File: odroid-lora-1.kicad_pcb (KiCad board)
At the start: 2 copper layers, 110 x 110 mm, 14 parts, among them J1 ODROID_2x12_GPIO, J2 RASPPI_2x20_GPIO, J3 M0, J4 M1

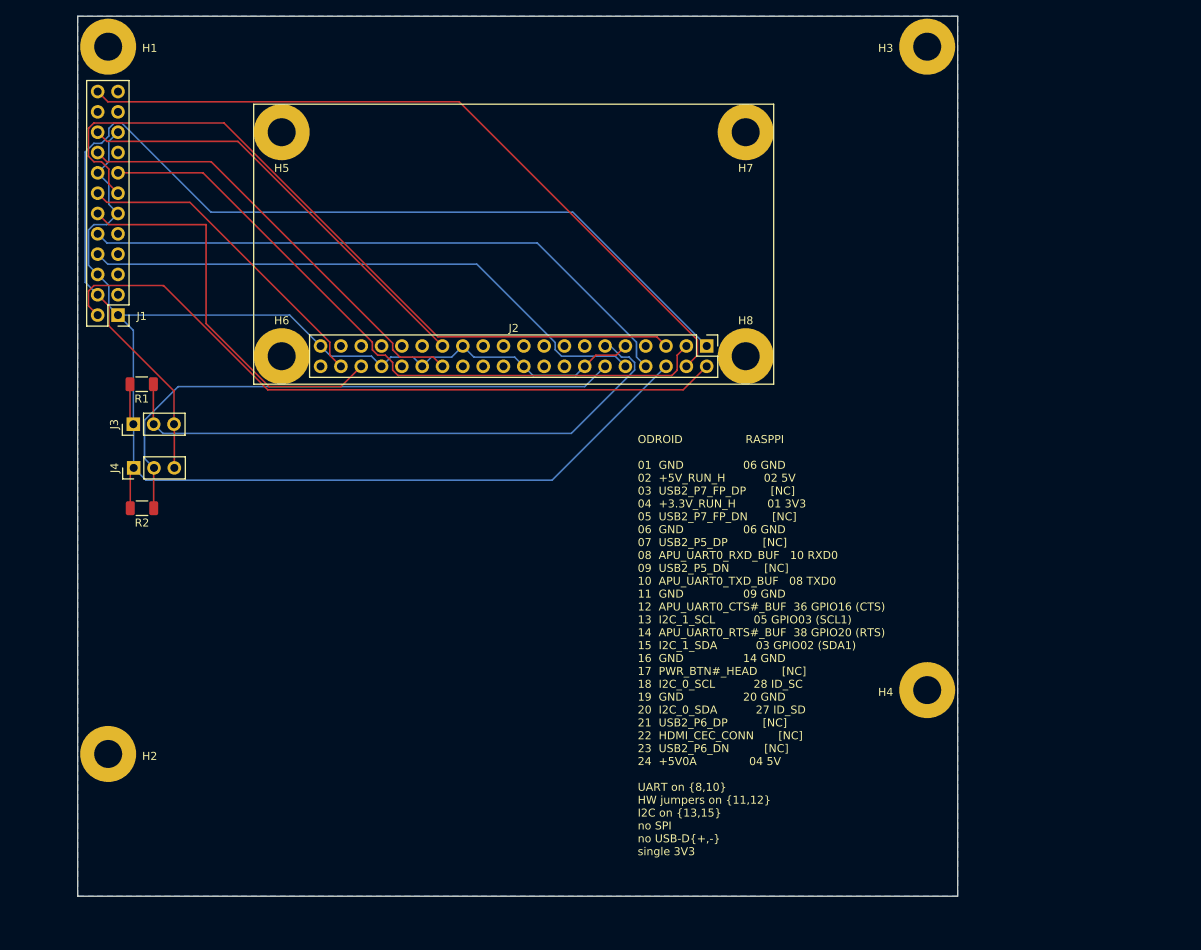
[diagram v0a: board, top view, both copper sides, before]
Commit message: update to angled condensed design
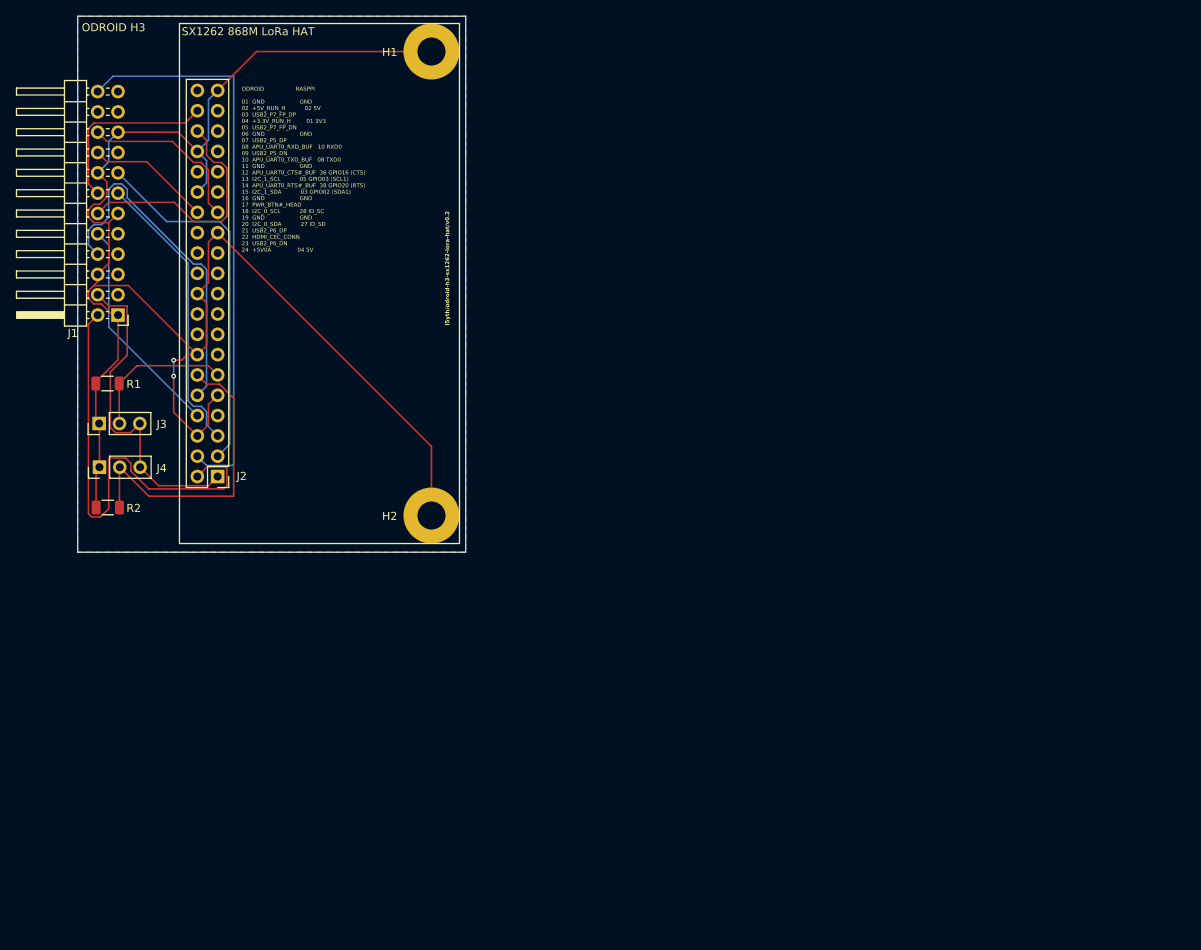
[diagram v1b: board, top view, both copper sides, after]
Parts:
- removed the H1 at (106.8, 42.3)
- removed the H2 at (106.8, 130.7)
- removed H3, H4: MountingOdroid, MountingHole:MountingHole_3.5mm_Pad
- removed H6, H8: MountingWaveshare, MountingHole:MountingHole_3.5mm_Pad
- H1: renamed from H5; value MountingWaveshare -> MountingHole_Pad
- H2: renamed from H7; value MountingWaveshare -> MountingHole_Pad
- J1: footprint Connector_PinHeader_2.54mm:PinHeader_2x12_P2.54mm_Vertical -> Connector_PinHeader_2.54mm:PinHeader_2x12_P2.54mm_Horizontal
- moved J2 63.3 mm to (120.5, 96.0), turned to 180 degrees
- moved H2 62.0 mm to (147.2, 100.9), turned to -90 degrees
- moved H1 21.3 mm to (147.2, 42.9), turned to -90 degrees
- moved J4 4.28 mm to (105.7, 94.9)
- moved R1 4.28 mm to (106.7, 84.4)
- moved J3 4.28 mm to (105.7, 89.4)
- moved R2 4.28 mm to (106.8, 99.9)
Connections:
- H1 pad 1: (no net) -> GND
- H2 pad 1: (no net) -> GND
- J2 pad 17: unconnected-(J2-Pin_17-Pad17) -> Net-(J1-Pin_4)
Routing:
- net Net-(J1-Pin_4): track 135.4 -> 41.4 mm
- net Net-(J1-Pin_13): track 94.2 -> 36.1 mm
- net Net-(J2-Pin_11): track 74.4 -> 19.3 mm
- net Net-(J1-Pin_10): track 76.5 -> 27.9 mm
- net Net-(J1-Pin_15): track 85.3 -> 45.7 mm
- net Net-(J1-Pin_18): track 54.7 -> 15.6 mm
- net Net-(J2-Pin_12): track 71.9 -> 38.8 mm
- net Net-(J1-Pin_20): track 54.2 -> 21.6 mm
- net Net-(J1-Pin_2): track 87.7 -> 58.3 mm
- net Net-(J1-Pin_8): track 72.3 -> 43.9 mm
- net Net-(J1-Pin_24): track 91.7 -> 71.4 mm
- net Net-(J1-Pin_12): track 50.2 -> 30.7 mm
- net Net-(J1-Pin_14): track 40.3 -> 23.1 mm
- net GND: track 203.5 -> 213.3 mm, vias 0 -> 2
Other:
- board size 110 x 110 mm -> 48.5 x 67 mm
- board text added: "ODROID H3"
- board text added: "ODROID RASPPI 01 GND GND 02 +5V_RUN_H 02 5V 03 USB2_P7_FP_DP 04 +3.3V_RUN_H 01 3V3 05 USB2_P7_FP_DN 06 GND GND 07 USB2_P5_DP 08 APU_UART0_RXD_BUF 10 RXD0 09 USB2_P5_DN 10 APU_UART0_TXD_BUF 08 TXD0 11 GND GND 12 APU_UART0_CTS#_BUF 36 GPIO16 (CTS) 13 I2C_1_SCL 05 GPIO03 (SCL1) 14 APU_UART0_RTS#_BUF 38 GPIO20 (RTS) 15 I2C_1_SDA 03 GPIO02 (SDA1) 16 GND GND 17 PWR_BTN#_HEAD 18 I2C_0_SCL 28 ID_SC 19 GN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"
- board text added: "SX1262 868M LoRa HAT"
- board text added: "l5yth/odroid-h3-sx1262-lora-hat/v0.2"
- board text removed: "ODROID RASPPI 01 GND 06 GND 02 +5V_RUN_H 02 5V 03 USB2_P7_FP_DP [NC] 04 +3.3V_RUN_H 01 3V3 05 USB2_P7_FP_DN [NC] 06 GND 06 GND 07 USB2_P5_DP [NC] 08 APU_UART0_RXD_BUF 10 RXD0 09 USB2_P5_DN [NC] 10 APU_UART0_TXD_BUF 08 TXD0 11 GND 09 GND 12 APU_UART0_CTS#_BUF 36 GPIO16 (CTS) 13 I2C_1_SCL 05 GPIO03 (SCL1) 14 APU_UART0_RTS#_BUF 38 GPIO20 (RTS) 15 I2C_1_SDA 03 GPIO02 (SDA1) 16 GND 14 GND 17 PWR_BTN#_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"

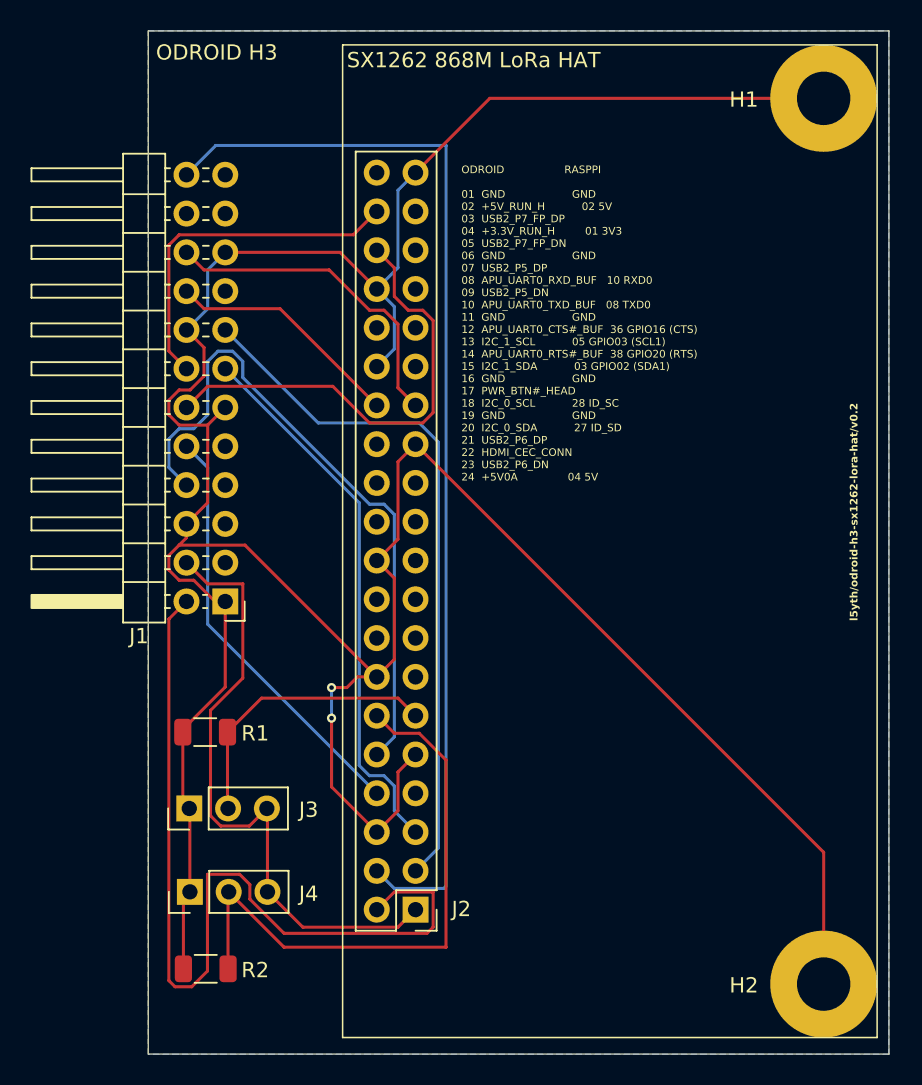
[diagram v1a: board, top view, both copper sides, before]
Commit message: replace pinheader with pinsocket for the odroid connector
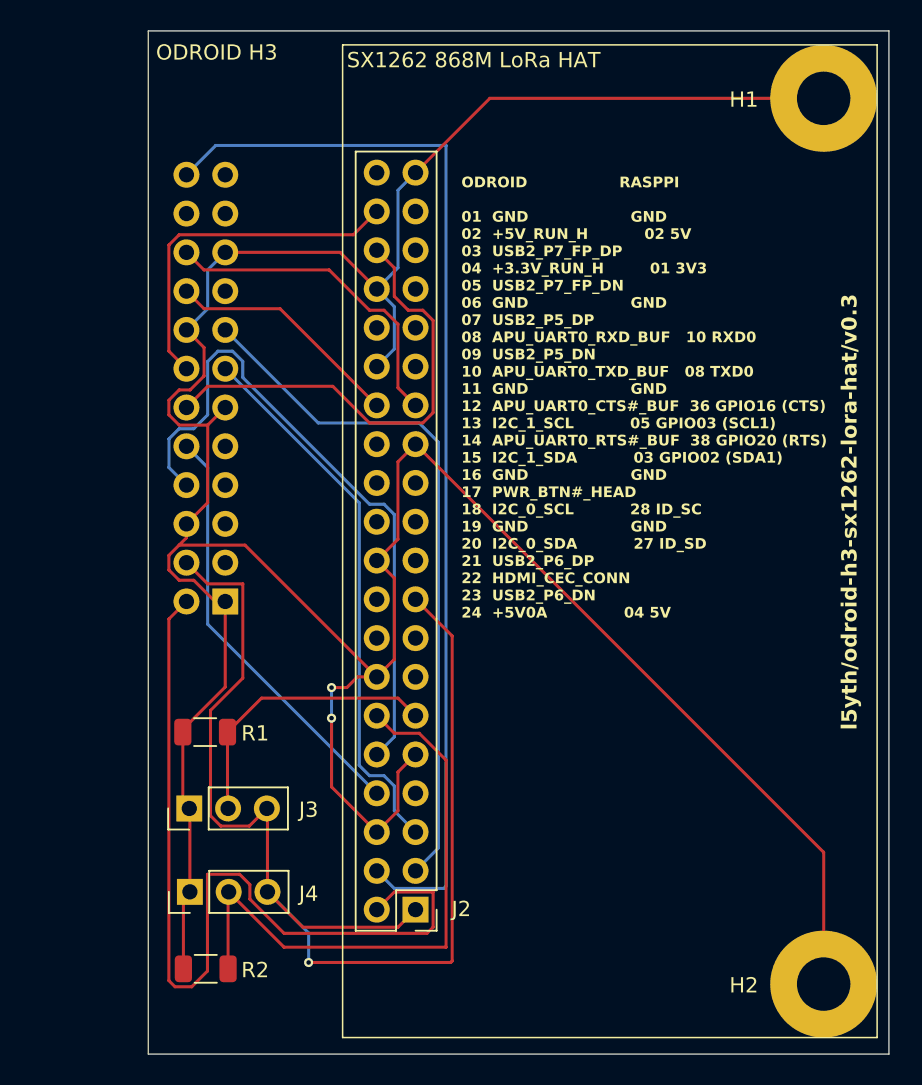
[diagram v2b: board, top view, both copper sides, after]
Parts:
- J1: footprint Connector_PinHeader_2.54mm:PinHeader_2x12_P2.54mm_Horizontal -> Connector_PinSocket_2.54mm:PinSocket_2x12_P2.54mm_Horizontal; moved to B.Cu
- turned J1 to 0 degrees
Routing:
- net Net-(J1-Pin_4): track 41.4 -> 81.2 mm, vias 0 -> 1
- removed copper zone on B.Cu, net GND
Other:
- board text added: "l5yth/odroid-h3-sx1262-lora-hat/v0.3"
- board text removed: "l5yth/odroid-h3-sx1262-lora-hat/v0.2"

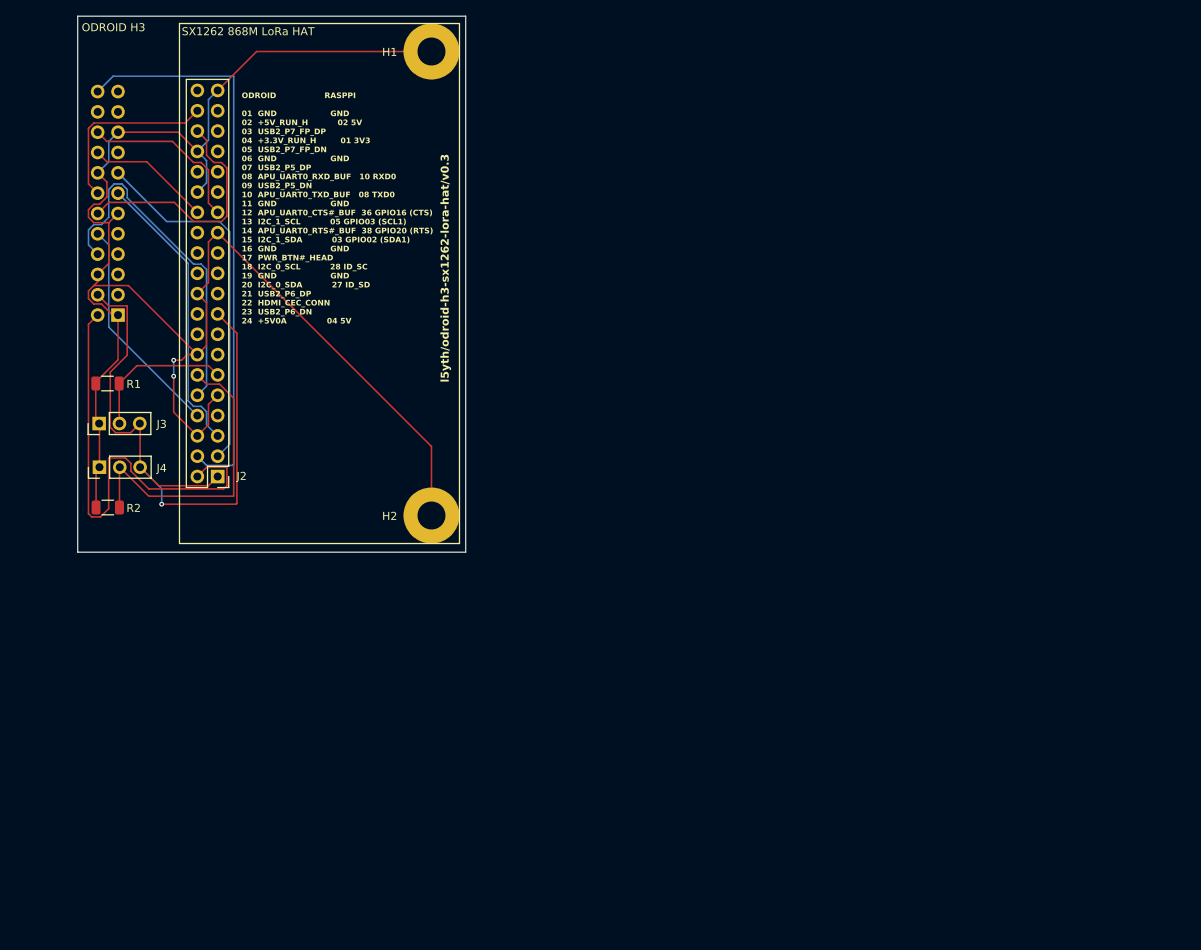
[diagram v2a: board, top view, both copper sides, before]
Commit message: define power nets and increase trace width for currents
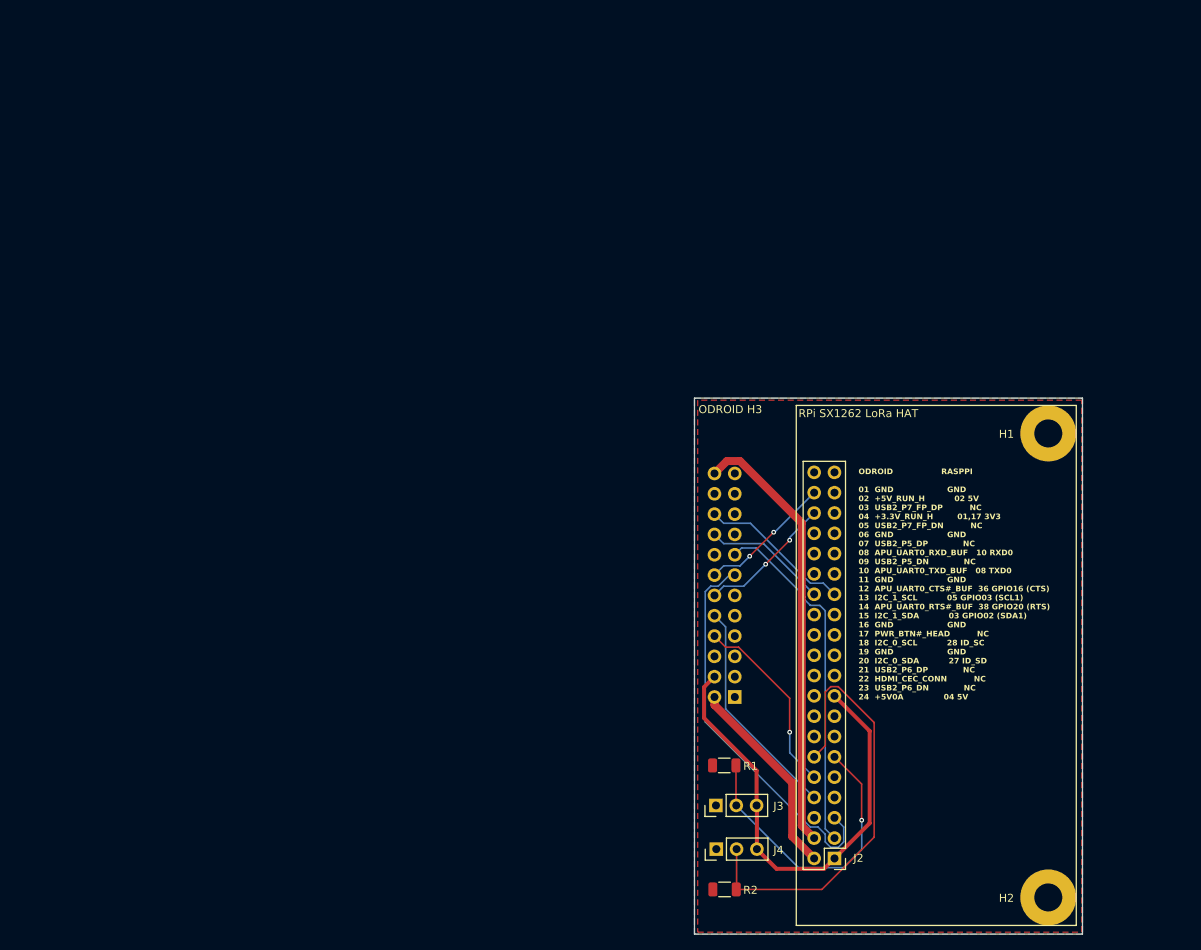
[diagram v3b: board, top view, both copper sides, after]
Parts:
- H1, H2: value MountingHole_Pad -> MountingHole_SX1268
- moved H1 90.7 mm to (224.3, 90.7)
- moved J4 90.7 mm to (182.8, 142.6)
- moved H2 90.7 mm to (224.3, 148.7)
- moved J1 90.7 mm to (185.1, 123.6)
- moved R1 90.7 mm to (183.8, 132.2)
- moved R2 90.7 mm to (183.9, 147.7)
- moved J2 90.7 mm to (197.6, 143.8)
- moved J3 90.7 mm to (182.8, 137.2)
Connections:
- net Net-(J1-Pin_2) renamed +5VA
- net Net-(J1-Pin_24) renamed +5VB
- net Net-(J1-Pin_4) renamed +3V3
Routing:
- net GND: track 213.3 -> 0.00 mm, vias 2 -> 0
- net +5VA: track 58.3 -> 25.3 mm
- net +3V3: track 81.2 -> 60.1 mm, vias 1 -> 0
- net Net-(J1-Pin_8): track 43.9 -> 23.8 mm, vias 0 -> 1
- net Net-(J2-Pin_11): track 19.3 -> 37.9 mm, vias 0 -> 1
- net Net-(J2-Pin_12): track 38.8 -> 56.2 mm
- net +5VB: track 71.4 -> 54.8 mm
- net Net-(J1-Pin_12): track 30.7 -> 16.9 mm, vias 0 -> 2
- net Net-(J1-Pin_13): track 36.1 -> 49.0 mm
- net Net-(J1-Pin_14): track 23.1 -> 16.7 mm, vias 0 -> 2
- net Net-(J1-Pin_20): track 21.6 -> 19.2 mm
- net Net-(J1-Pin_15): track 45.7 -> 44.1 mm
- added copper zone on B.Cu, net GND
- added copper zone on F.Cu, net GND
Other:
- board text added: "ODROID RASPPI 01 GND GND 02 +5V_RUN_H 02 5V 03 USB2_P7_FP_DP NC 04 +3.3V_RUN_H 01,17 3V3 05 USB2_P7_FP_DN NC 06 GND GND 07 USB2_P5_DP NC 08 APU_UART0_RXD_BUF 10 RXD0 09 USB2_P5_DN NC 10 APU_UART0_TXD_BUF 08 TXD0 11 GND GND 12 APU_UART0_CTS#_BUF 36 GPIO16 (CTS) 13 I2C_1_SCL 05 GPIO03 (SCL1) 14 APU_UART0_RTS#_BUF 38 GPIO20 (RTS) 15 I2C_1_SDA 03 GPIO02 (SDA1) 16 GND GND 17 PWR_BTN#_HEAD NC 18 I2C_0_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"
- board text added: "RPi SX1262 LoRa HAT"
- board text added: "l5yth/odroid-h3-sx1262-lora-hat/v0.4"
- board text removed: "ODROID RASPPI 01 GND GND 02 +5V_RUN_H 02 5V 03 USB2_P7_FP_DP 04 +3.3V_RUN_H 01 3V3 05 USB2_P7_FP_DN 06 GND GND 07 USB2_P5_DP 08 APU_UART0_RXD_BUF 10 RXD0 09 USB2_P5_DN 10 APU_UART0_TXD_BUF 08 TXD0 11 GND GND 12 APU_UART0_CTS#_BUF 36 GPIO16 (CTS) 13 I2C_1_SCL 05 GPIO03 (SCL1) 14 APU_UART0_RTS#_BUF 38 GPIO20 (RTS) 15 I2C_1_SDA 03 GPIO02 (SDA1) 16 GND GND 17 PWR_BTN#_HEAD 18 I2C_0_SCL 28 ID_SC 19 GN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"
- board text removed: "SX1262 868M LoRa HAT"
- board text removed: "l5yth/odroid-h3-sx1262-lora-hat/v0.3"

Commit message: add fuses
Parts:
- added F1: Fuse_2A, Fuse:Fuse_1206_3216Metric, F.Cu at (185.0, 111.0)
- added F2: Fuse_2A, Fuse:Fuse_1206_3216Metric, F.Cu at (198.0, 96.0)
- H1, H2: value MountingHole_SX1268 -> MOUNT_SX1268
- J1: value ODROID_2x12_GPIO -> ODROID_2x12_SOCKET
- J2: value RASPPI_2x20_GPIO -> RASPPI_2x20_HEADER
- J3: value M0 -> Mode0
- J4: value M1 -> Mode1
- R1, R2: value 47K -> 51K
- moved H1 58.7 mm to (236.8, 148.0), turned to 180 degrees
- moved R2 52.0 mm to (178.5, 96.0), turned to 90 degrees
- moved J4 47.7 mm to (183.5, 94.9), turned to 0 degrees
- moved H2 45.5 mm to (178.8, 148.0), turned to 180 degrees
- moved J3 42.7 mm to (189.0, 94.9), turned to 0 degrees
- moved R1 37.6 mm to (194.0, 95.9), turned to 90 degrees
- moved J1 32.7 mm to (204.4, 97.1), turned to -90 degrees
- moved J2 26.4 mm to (183.7, 121.3), turned to 90 degrees
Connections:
- net +3V3 renamed /3V_RUN_H
- net GND renamed /GND
- net Net-(J1-Pin_10) renamed /UART0_TXD
- net Net-(J1-Pin_12) renamed /UART0_CTS
- net Net-(J1-Pin_13) renamed /I2C1_SCL
- net Net-(J1-Pin_14) renamed /UART0_RTS
- net Net-(J1-Pin_15) renamed /I2C1_SDA
- net Net-(J1-Pin_18) renamed /I2C0_SCL
- net Net-(J1-Pin_20) renamed /I2C0_SDA
- net Net-(J1-Pin_8) renamed /UART0_RXD
- net Net-(J2-Pin_11) renamed /GPIO_M0
- net Net-(J2-Pin_12) renamed /GPIO_M1
- J1 pad 2: +5VA -> /5V_RUN_H
- J1 pad 24: +5VB -> unconnected-(J1-Pin_24-Pad24)
- J2 pad 2: +5VA -> /5V_RUN_H
- J2 pad 4: +5VB -> /5V_RUN_H
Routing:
- net +5VB: track 54.8 -> 0.00 mm
- net /5V_RUN_H: track 0.00 -> 39.4 mm
- net +5VA: track 25.3 -> 0.00 mm
- net /GPIO_M1: track 56.2 -> 31.7 mm
- net /3V_RUN_H: track 60.1 -> 74.7 mm
- net /I2C0_SDA: track 19.2 -> 31.1 mm
- net /I2C0_SCL: track 15.6 -> 27.5 mm
- net /UART0_RTS: track 16.7 -> 28.2 mm, vias 2 -> 0
- net /UART0_CTS: track 16.9 -> 28.2 mm, vias 2 -> 0
- net /UART0_TXD: track 27.9 -> 37.2 mm
- net /I2C1_SDA: track 44.1 -> 53.0 mm
- net /UART0_RXD: track 23.8 -> 31.7 mm, vias 1 -> 0
- net /I2C1_SCL: track 49.0 -> 42.9 mm
- net /GPIO_M0: track 37.9 -> 32.9 mm, vias 1 -> 0
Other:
- board size 48.5 x 67 mm -> 67 x 61.5 mm
- board text added: "ODROID RASPPI 01 GND GND 02 +5V_RUN_H 02,04 5V 03 USB2_P7_FP_DP NC 04 +3.3V_RUN_H 01,17 3V3 05 USB2_P7_FP_DN NC 06 GND GND 07 USB2_P5_DP NC 08 APU_UART0_RXD_BUF 10 RXD0 09 USB2_P5_DN NC 10 APU_UART0_TXD_BUF 08 TXD0 11 GND GND 12 APU_UART0_CTS#_BUF 36 GPIO16 (CTS) 13 I2C_1_SCL 05 GPIO03 (SCL1) 14 APU_UART0_RTS#_BUF 38 GPIO20 (RTS) 15 I2C_1_SDA 03 GPIO02 (SDA1) 16 GND GND 17 PWR_BTN#_HEAD NC 18 I2C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"
- board text removed: "ODROID RASPPI 01 GND GND 02 +5V_RUN_H 02 5V 03 USB2_P7_FP_DP NC 04 +3.3V_RUN_H 01,17 3V3 05 USB2_P7_FP_DN NC 06 GND GND 07 USB2_P5_DP NC 08 APU_UART0_RXD_BUF 10 RXD0 09 USB2_P5_DN NC 10 APU_UART0_TXD_BUF 08 TXD0 11 GND GND 12 APU_UART0_CTS#_BUF 36 GPIO16 (CTS) 13 I2C_1_SCL 05 GPIO03 (SCL1) 14 APU_UART0_RTS#_BUF 38 GPIO20 (RTS) 15 I2C_1_SDA 03 GPIO02 (SDA1) 16 GND GND 17 PWR_BTN#_HEAD NC 18 I2C_0_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"
